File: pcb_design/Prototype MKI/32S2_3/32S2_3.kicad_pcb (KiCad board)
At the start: 2 copper layers, 16 parts, among them J1 Conn_01x08, U1 AT30TS74, U2 NCU18XH103F60RB, U3 ESP32_S2_SOLO, U4 RP402N331F-TR-FE

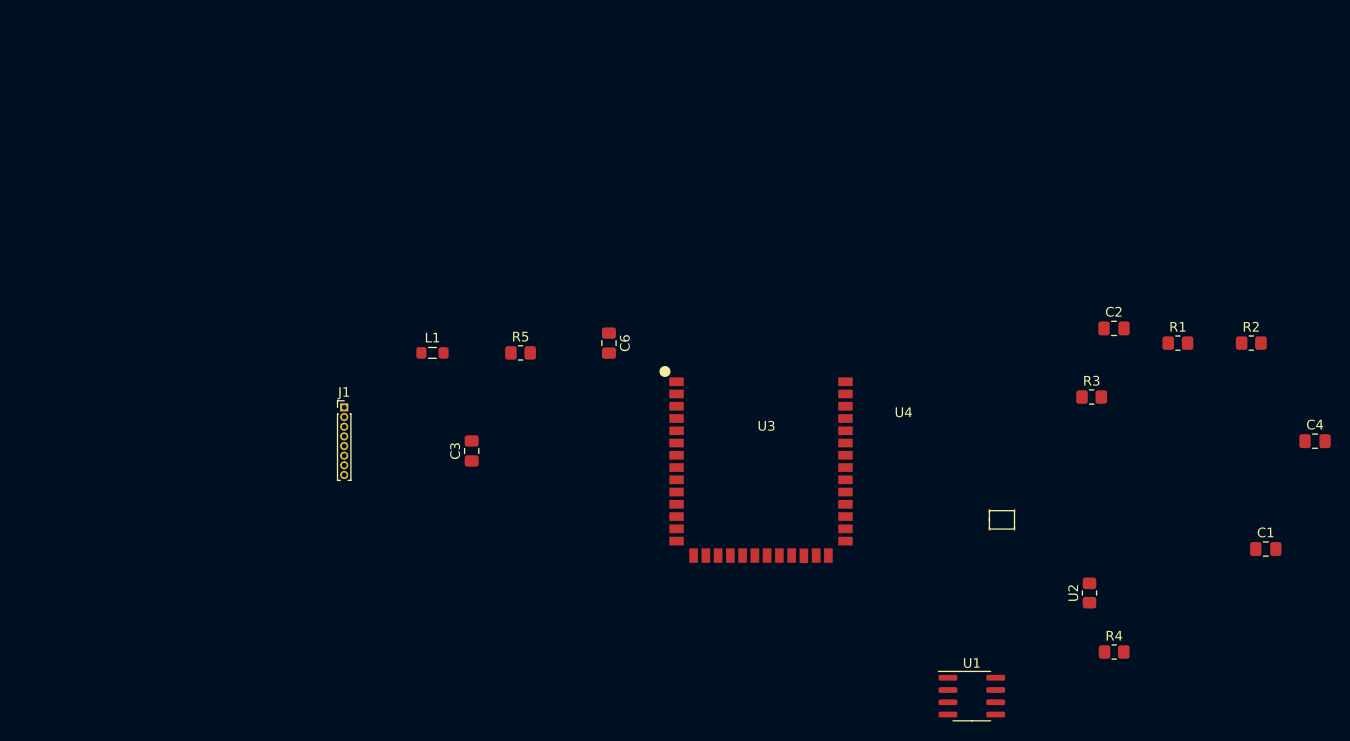
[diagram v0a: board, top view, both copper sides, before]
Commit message: Added Programming board
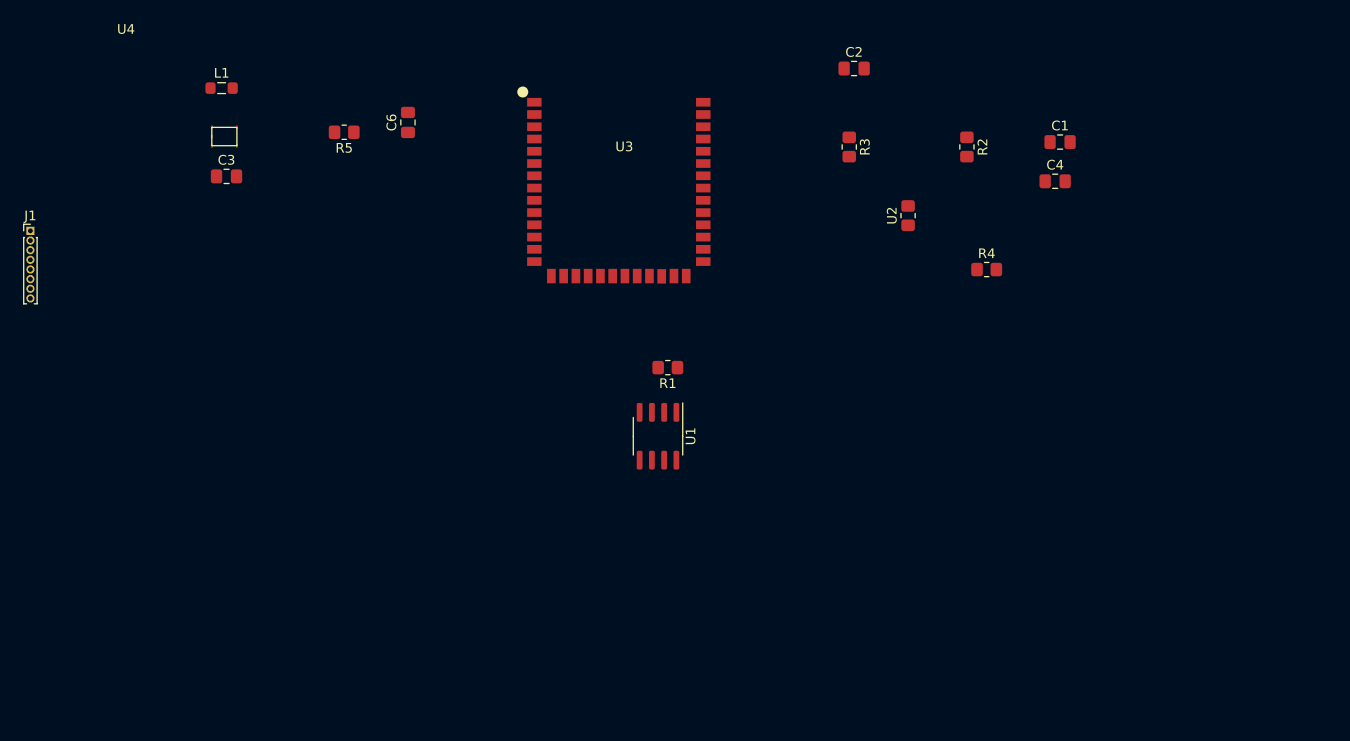
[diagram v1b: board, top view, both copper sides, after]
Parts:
- moved U4 89.8 mm to (35.1, 46.2)
- moved R1 52.9 mm to (82.3, 71.1), turned to 180 degrees
- moved C1 47.2 mm to (122.9, 47.8)
- moved U2 43.4 mm to (107.2, 55.4)
- moved U1 42.2 mm to (81.3, 78.2), turned to -90 degrees
- moved R4 41.8 mm to (115.3, 61.0)
- moved C3 38.1 mm to (36.6, 51.3), turned to 0 degrees
- moved C2 38.1 mm to (101.6, 40.1)
- moved C4 38.1 mm to (122.4, 51.8)
- moved J1 37.3 mm to (16.3, 57.0)
- moved R3 36.1 mm to (101.1, 48.3), turned to -90 degrees
- moved R2 35.8 mm to (113.3, 48.3), turned to -90 degrees
- moved L1 35.1 mm to (36.1, 42.2)
- moved U3 32.5 mm to (68.5, 43.6)
- moved C6 30.9 mm to (55.4, 45.7), turned to 90 degrees
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
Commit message: v1 of PCB layout done
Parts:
- moved J1 90.4 mm to (104.8, 75.2)
- moved C4 61.3 mm to (70.5, 84.5), turned to 180 degrees
- moved U4 53.5 mm to (69.3, 87.3)
- moved C1 53.4 mm to (75.6, 72.4), turned to 180 degrees
- moved C3 52.5 mm to (70.5, 91.4)
- moved L1 52.1 mm to (70.5, 81.3)
- moved R2 51.6 mm to (92.1, 95.2), turned to 90 degrees
- moved R4 50.4 mm to (76.2, 92.7), turned to -90 degrees
- moved R3 47.2 mm to (97.2, 95.2), turned to 90 degrees
- moved U2 46.2 mm to (80.0, 92.7)
- moved R5 44.2 mm to (75.6, 81.9)
- moved C2 44.0 mm to (75.6, 75.6), turned to 180 degrees
- moved C6 38.7 mm to (75.6, 78.7), turned to 180 degrees
- moved U3 32.5 mm to (83.2, 72.6)
- moved R1 26.3 mm to (70.5, 94.6)
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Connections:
- J1 pad 6: /U0RXD -> /U0TXD
- J1 pad 7: /U0TXD -> /U0RXD
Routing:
- net /VCC_3V3: track 0.00 -> 99.6 mm
- net /CHIP_PU: track 0.00 -> 54.5 mm, vias 0 -> 2
- net VCC: track 0.00 -> 50.5 mm, vias 0 -> 2
- net /Vtherm: track 0.00 -> 49.6 mm, vias 0 -> 2
- net GND: track 0.00 -> 39.1 mm, vias 0 -> 7
- net Net-(R1-Pad2): track 0.00 -> 21.1 mm
- net /SDA: track 0.00 -> 17.1 mm
- net /SCL: track 0.00 -> 16.3 mm
- net /GPIO0: track 0.00 -> 13.2 mm
- net Net-(C1-Pad1): track 0.00 -> 10.4 mm
- net Net-(L1-Pad1): track 0.00 -> 6.69 mm
- net /U0TXD: track 0.00 -> 6.36 mm
- net /U0RXD: track 0.00 -> 6.20 mm
- added copper zone on B.Cu, net GND
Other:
- board outline added: 43.2 x 36.2 mm
